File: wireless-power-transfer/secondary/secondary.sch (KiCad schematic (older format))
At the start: 9 parts, among them J1 Screw_Terminal_1x02, J2 Screw_Terminal_1x02, U1 LM7812CT

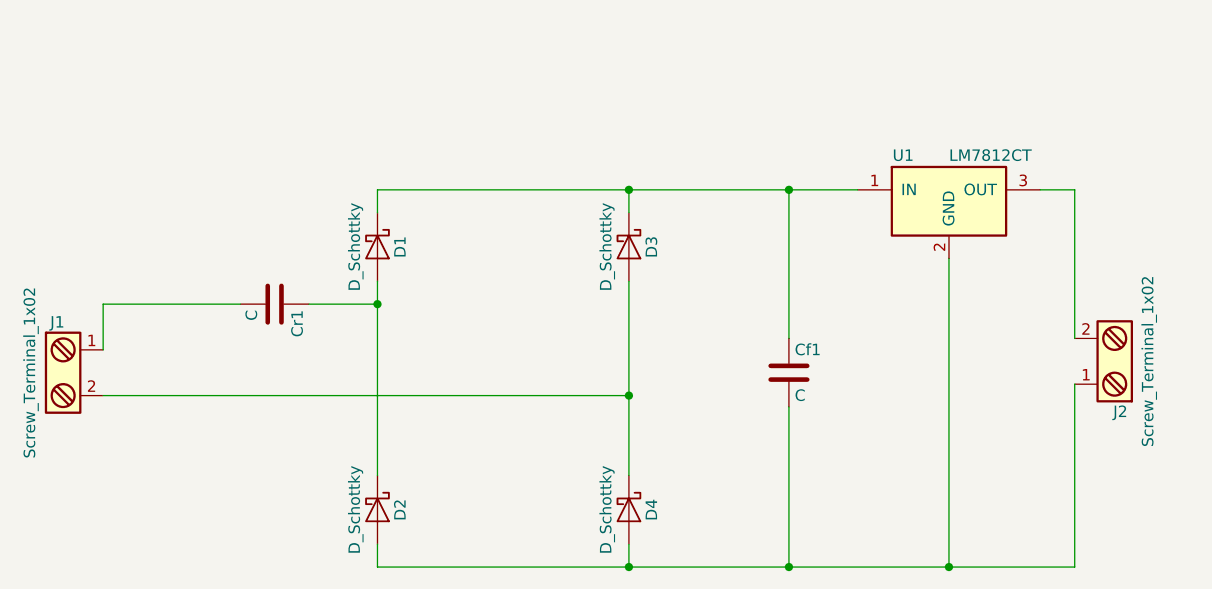
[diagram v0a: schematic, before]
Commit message: Added pdf sheets and modified layout according with the school standard for TFGs.
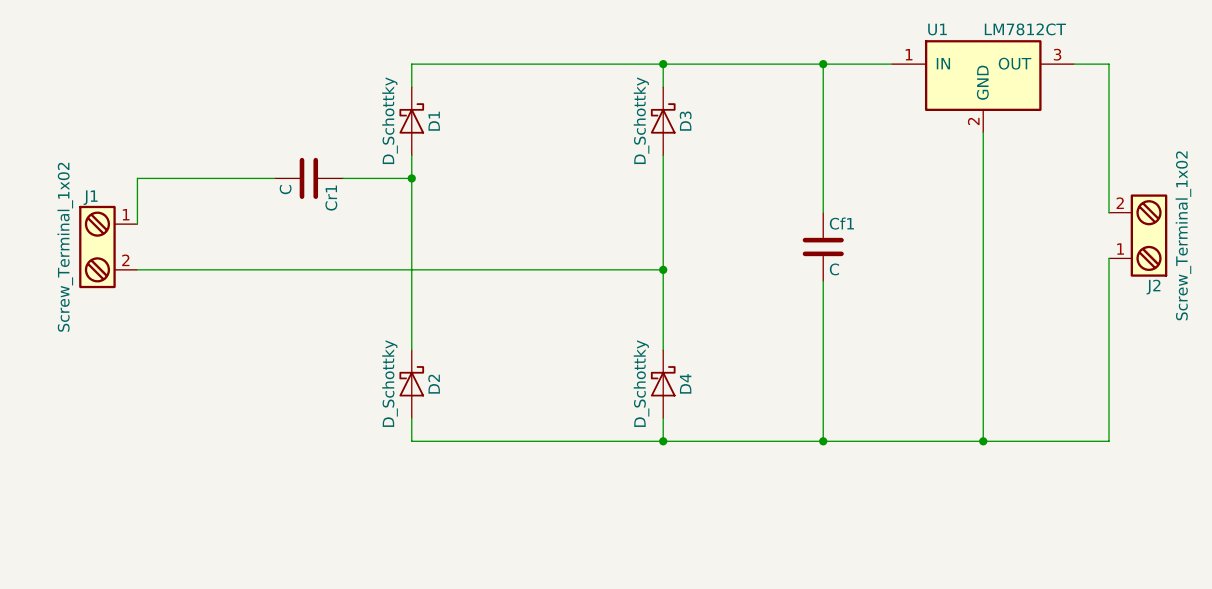
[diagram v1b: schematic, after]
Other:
- moved on the sheet: Cf1, Cr1, D1, D2, D3, D4, J1, J2, U1
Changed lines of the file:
@@
 L D_Schottky D1
 U 1 1 59E7A3A2
-P 4400 3100
-F 0 "D1" H 4400 3200 50  0000 C CNN
-F 1 "D_Schottky" H 4400 3000 50  0000 C CNN
-F 2 "Diodes_THT:D_DO-201AD_P12.70mm_Horizontal" H 4400 3100 50  0001 C CNN
-F 3 "" H 4400 3100 50  0001 C CNN
-	1    4400 3100
+P 4550 2550
+F 0 "D1" H 4550 2650 50  0000 C CNN
+F 1 "D_Schottky" H 4550 2450 50  0000 C CNN
+F 2 "Diodes_THT:D_DO-201AD_P12.70mm_Horizontal" H 4550 2550 50  0001 C CNN
+F 3 "" H 4550 2550 50  0001 C CNN
+	1    4550 2550
 	0    1    1    0
 $EndComp
@@
 L D_Schottky D2
 U 1 1 59E7A526
-P 4400 4250
-F 0 "D2" H 4400 4350 50  0000 C CNN
-F 1 "D_Schottky" H 4400 4150 50  0000 C CNN
-F 2 "Diodes_THT:D_DO-201AD_P12.70mm_Horizontal" H 4400 4250 50  0001 C CNN
-F 3 "" H 4400 4250 50  0001 C CNN
-	1    4400 4250
+P 4550 3700
+F 0 "D2" H 4550 3800 50  0000 C CNN
+F 1 "D_Schottky" H 4550 3600 50  0000 C CNN
+F 2 "Diodes_THT:D_DO-201AD_P12.70mm_Horizontal" H 4550 3700 50  0001 C CNN
+F 3 "" H 4550 3700 50  0001 C CNN
+	1    4550 3700
 	0    1    1    0
 $EndComp
@@
 L D_Schottky D3
 U 1 1 59E7A56E
-P 5500 3100
-F 0 "D3" H 5500 3200 50  0000 C CNN
-F 1 "D_Schottky" H 5500 3000 50  0000 C CNN
-F 2 "Diodes_THT:D_DO-201AD_P12.70mm_Horizontal" H 5500 3100 50  0001 C CNN
-F 3 "" H 5500 3100 50  0001 C CNN
-	1    5500 3100
+P 5650 2550
+F 0 "D3" H 5650 2650 50  0000 C CNN
+F 1 "D_Schottky" H 5650 2450 50  0000 C CNN
+F 2 "Diodes_THT:D_DO-201AD_P12.70mm_Horizontal" H 5650 2550 50  0001 C CNN
+F 3 "" H 5650 2550 50  0001 C CNN
+	1    5650 2550
 	0    1    1    0
 $EndComp
@@
 L D_Schottky D4
 U 1 1 59E7A5B1
-P 5500 4250
-F 0 "D4" H 5500 4350 50  0000 C CNN
-F 1 "D_Schottky" H 5500 4150 50  0000 C CNN
-F 2 "Diodes_THT:D_DO-201AD_P12.70mm_Horizontal" H 5500 4250 50  0001 C CNN
-F 3 "" H 5500 4250 50  0001 C CNN
-	1    5500 4250
+P 5650 3700
+F 0 "D4" H 5650 3800 50  0000 C CNN
+F 1 "D_Schottky" H 5650 3600 50  0000 C CNN
+F 2 "Diodes_THT:D_DO-201AD_P12.70mm_Horizontal" H 5650 3700 50  0001 C CNN
+F 3 "" H 5650 3700 50  0001 C CNN
+	1    5650 3700
 	0    1    1    0
 $EndComp
@@
 L C Cr1
 U 1 1 59E7A649
-P 3950 3350
-F 0 "Cr1" H 3975 3450 50  0000 L CNN
-F 1 "C" H 3975 3250 50  0000 L CNN
-F 2 "Capacitors_THT:C_Axial_L5.1mm_D3.1mm_P7.50mm_Horizontal" H 3988 3200 50  0001 C CNN
-F 3 "" H 3950 3350 50  0001 C CNN
-	1    3950 3350
+P 4100 2800
+F 0 "Cr1" H 4125 2900 50  0000 L CNN
+F 1 "C" H 4125 2700 50  0000 L CNN
+F 2 "Capacitors_THT:C_Axial_L5.1mm_D3.1mm_P7.50mm_Horizontal" H 4138 2650 50  0001 C CNN
+F 3 "" H 4100 2800 50  0001 C CNN
+	1    4100 2800
 	0    1    1    0
 $EndComp
@@
 L Screw_Terminal_1x02 J1
 U 1 1 59E7A6B3
-P 3000 3650
-F 0 "J1" H 3000 3900 50  0000 C TNN
-F 1 "Screw_Terminal_1x02" V 2850 3650 50  0000 C TNN
-F 2 "Connectors_Terminal_Blocks:TerminalBlock_Pheonix_MKDS1.5-2pol" H 3000 3425 50  0001 C CNN
-F 3 "" H 2975 3650 50  0001 C CNN
-	1    3000 3650
+P 3150 3100
+F 0 "J1" H 3150 3350 50  0000 C TNN
+F 1 "Screw_Terminal_1x02" V 3000 3100 50  0000 C TNN
+F 2 "Connectors_Terminal_Blocks:TerminalBlock_Pheonix_MKDS1.5-2pol" H 3150 2875 50  0001 C CNN
+F 3 "" H 3125 3100 50  0001 C CNN
+	1    3150 3100
 	1    0    0    -1
 $EndComp
@@
 L C Cf1
 U 1 1 59E7A7AC
-P 6200 3650
-F 0 "Cf1" H 6225 3750 50  0000 L CNN
-F 1 "C" H 6225 3550 50  0000 L CNN
-F 2 "Capacitors_THT:C_Rect_L13.0mm_W5.0mm_P10.00mm_FKS3_FKP3_MKS4" H 6238 3500 50  0001 C CNN
-F 3 "" H 6200 3650 50  0001 C CNN
-	1    6200 3650
+P 6350 3100
+F 0 "Cf1" H 6375 3200 50  0000 L CNN
+F 1 "C" H 6375 3000 50  0000 L CNN
+F 2 "Capacitors_THT:C_Rect_L13.0mm_W5.0mm_P10.00mm_FKS3_FKP3_MKS4" H 6388 2950 50  0001 C CNN
+F 3 "" H 6350 3100 50  0001 C CNN
+	1    6350 3100
 	1    0    0    -1
 $EndComp
@@
 L LM7812CT U1
 U 1 1 59E7A939
-P 6900 2900
-F 0 "U1" H 6700 3100 50  0000 C CNN
-F 1 "LM7812CT" H 6900 3100 50  0000 L CNN
-F 2 "TO_SOT_Packages_THT:TO-220-3_Vertical" H 6900 3000 50  0001 C CIN
-F 3 "" H 6900 2900 50  0001 C CNN
-	1    6900 2900
+P 7050 2350
+F 0 "U1" H 6850 2550 50  0000 C CNN
+F 1 "LM7812CT" H 7050 2550 50  0000 L CNN
+F 2 "TO_SOT_Packages_THT:TO-220-3_Vertical" H 7050 2450 50  0001 C CIN
+F 3 "" H 7050 2350 50  0001 C CNN
+	1    7050 2350
 	1    0    0    -1
 $EndComp
 Wire Wire Line
-	4400 4100 4400 3250
+	4550 3550 4550 2700
 Wire Wire Line
-	5500 3250 5500 4100
+	5650 2700 5650 3550
 Wire Wire Line
-	3200 3550 3200 3350
+	3350 3000 3350 2800
 Wire Wire Line
-	3200 3350 3800 3350
+	3350 2800 3950 2800
 Wire Wire Line
-	4400 2950 4400 2850
+	4550 2400 4550 2300
 Wire Wire Line
-	4400 2850 6500 2850
+	4550 2300 6650 2300
 Wire Wire Line
-	5500 2850 5500 2950
+	5650 2300 5650 2400
 Wire Wire Line
-	4400 4400 4400 4500
+	4550 3850 4550 3950
 Wire Wire Line
-	4400 4500 7450 4500
+	4550 3950 7600 3950
 Wire Wire Line
-	5500 4500 5500 4400
+	5650 3950 5650 3850
 Wire Wire Line
-	4100 3350 4400 3350
-Connection ~ 4400 3350
+	4250 2800 4550 2800
+Connection ~ 4550 2800
 Wire Wire Line
-	3200 3750 5500 3750
-Connection ~ 5500 3750
+	3350 3200 5650 3200
+Connection ~ 5650 3200
 Wire Wire Line
-	6200 2850 6200 3500
-Connection ~ 5500 2850
+	6350 2300 6350 2950
+Connection ~ 5650 2300
 Wire Wire Line
-	6200 4500 6200 3800
-Connection ~ 5500 4500
-Connection ~ 6200 2850
+	6350 3950 6350 3250
+Connection ~ 5650 3950
+Connection ~ 6350 2300
 Wire Wire Line
-	6900 4500 6900 3150
-Connection ~ 6200 4500
+	7050 3950 7050 2600
+Connection ~ 6350 3950
 $Comp
 L Screw_Terminal_1x02 J2
 U 1 1 59E7AA22
-P 7650 3600
-F 0 "J2" H 7650 3850 50  0000 C TNN
-F 1 "Screw_Terminal_1x02" V 7500 3600 50  0000 C TNN
-F 2 "Connectors_Terminal_Blocks:TerminalBlock_Pheonix_MKDS1.5-2pol" H 7650 3375 50  0001 C CNN
-F 3 "" H 7625 3600 50  0001 C CNN
-	1    7650 3600
+P 7800 3050
+F 0 "J2" H 7800 3300 50  0000 C TNN
+F 1 "Screw_Terminal_1x02" V 7650 3050 50  0000 C TNN
+F 2 "Connectors_Terminal_Blocks:TerminalBlock_Pheonix_MKDS1.5-2pol" H 7800 2825 50  0001 C CNN
+F 3 "" H 7775 3050 50  0001 C CNN
+	1    7800 3050
 	-1   0    0    1
 $EndComp
 Wire Wire Line
-	7300 2850 7450 2850
+	7450 2300 7600 2300
 Wire Wire Line
-	7450 2850 7450 3500
+	7600 2300 7600 2950
 Wire Wire Line
-	7450 4500 7450 3700
-Connection ~ 6900 4500
+	7600 3950 7600 3150
+Connection ~ 7050 3950
 $EndSCHEMATC

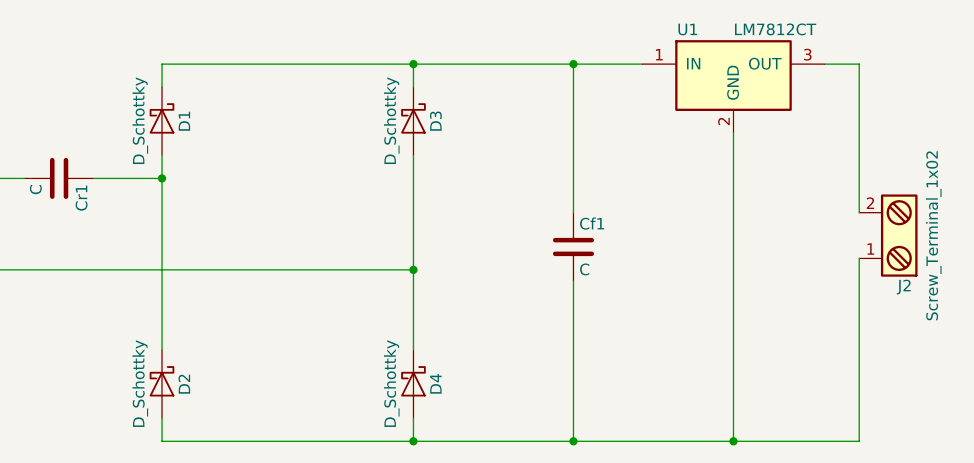
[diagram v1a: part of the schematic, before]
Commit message: Modified secondary PCB for better fitting in the car.
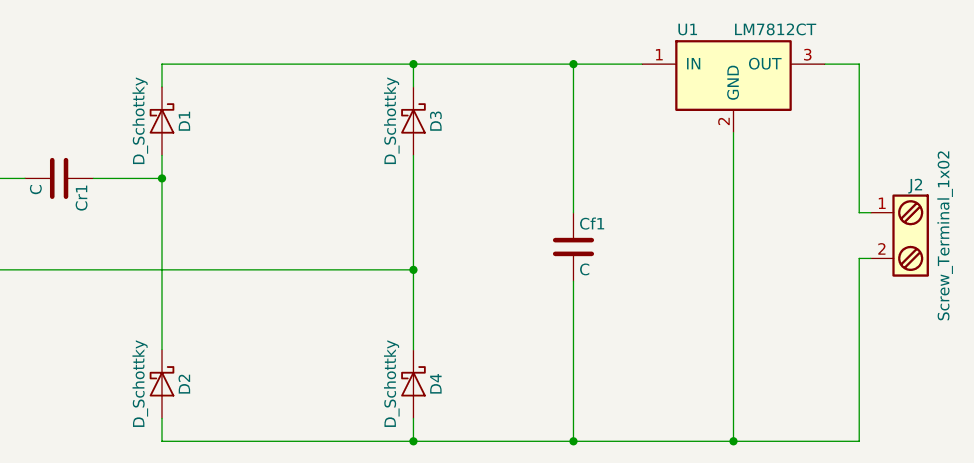
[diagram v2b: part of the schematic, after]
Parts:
- Cf1: footprint Capacitors_THT:C_Rect_L13.0mm_W5.0mm_P10.00mm_FKS3_FKP3_MKS4 -> Capacitors_THT:CP_Radial_D8.0mm_P3.50mm
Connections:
- net at Cf1.2, D2.2 (A), D4.2 (A)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: now also J2.2; no longer J2.1
- net at U1.3 (OUT): now also J2.1; no longer J2.2
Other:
- moved on the sheet: J2
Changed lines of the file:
@@
 F 0 "Cf1" H 6375 3200 50  0000 L CNN
 F 1 "C" H 6375 3000 50  0000 L CNN
-F 2 "Capacitors_THT:C_Rect_L13.0mm_W5.0mm_P10.00mm_FKS3_FKP3_MKS4" H 6388 2950 50  0001 C CNN
+F 2 "Capacitors_THT:CP_Radial_D8.0mm_P3.50mm" H 6388 2950 50  0001 C CNN
 F 3 "" H 6350 3100 50  0001 C CNN
 	1    6350 3100
@@
 $EndComp
 Wire Wire Line
-	4550 3550 4550 2700
+	4550 2700 4550 3550
 Wire Wire Line
 	5650 2700 5650 3550
@@
 L Screw_Terminal_1x02 J2
 U 1 1 59E7AA22
-P 7800 3050
-F 0 "J2" H 7800 3300 50  0000 C TNN
-F 1 "Screw_Terminal_1x02" V 7650 3050 50  0000 C TNN
-F 2 "Connectors_Terminal_Blocks:TerminalBlock_Pheonix_MKDS1.5-2pol" H 7800 2825 50  0001 C CNN
-F 3 "" H 7775 3050 50  0001 C CNN
-	1    7800 3050
-	-1   0    0    1
+P 7850 3050
+F 0 "J2" H 7850 3300 50  0000 C TNN
+F 1 "Screw_Terminal_1x02" V 7700 3050 50  0000 C TNN
+F 2 "Connectors_Terminal_Blocks:TerminalBlock_Pheonix_MKDS1.5-2pol" H 7850 2825 50  0001 C CNN
+F 3 "" H 7825 3050 50  0001 C CNN
+	1    7850 3050
+	-1   0    0    -1
 $EndComp
 Wire Wire Line
 	7450 2300 7600 2300
+Connection ~ 7050 3950
 Wire Wire Line
 	7600 2300 7600 2950
 Wire Wire Line
-	7600 3950 7600 3150
-Connection ~ 7050 3950
+	7600 2950 7650 2950
+Wire Wire Line
+	7650 3150 7600 3150
+Wire Wire Line
+	7600 3150 7600 3950
 $EndSCHEMATC

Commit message: PDFs created with schematics and PCB layers for front and back sides.
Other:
- note added: "5/7"
- moved on the sheet: Cf1, Cr1, D1, D2, D3, D4, J1, J2, U1
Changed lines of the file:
@@
 EELAYER 25 0
 EELAYER END
-$Descr A4 11693 8268
+$Descr A4 8268 11693 portrait
 encoding utf-8
 Sheet 1 1
@@
 L D_Schottky D1
 U 1 1 59E7A3A2
-P 4550 2550
-F 0 "D1" H 4550 2650 50  0000 C CNN
-F 1 "D_Schottky" H 4550 2450 50  0000 C CNN
-F 2 "Diodes_THT:D_DO-201AD_P12.70mm_Horizontal" H 4550 2550 50  0001 C CNN
-F 3 "" H 4550 2550 50  0001 C CNN
-	1    4550 2550
+P 3175 4275
+F 0 "D1" H 3175 4375 50  0000 C CNN
+F 1 "D_Schottky" H 3175 4175 50  0000 C CNN
+F 2 "Diodes_THT:D_DO-201AD_P12.70mm_Horizontal" H 3175 4275 50  0001 C CNN
+F 3 "" H 3175 4275 50  0001 C CNN
+	1    3175 4275
 	0    1    1    0
 $EndComp
@@
 L D_Schottky D2
 U 1 1 59E7A526
-P 4550 3700
-F 0 "D2" H 4550 3800 50  0000 C CNN
-F 1 "D_Schottky" H 4550 3600 50  0000 C CNN
-F 2 "Diodes_THT:D_DO-201AD_P12.70mm_Horizontal" H 4550 3700 50  0001 C CNN
-F 3 "" H 4550 3700 50  0001 C CNN
-	1    4550 3700
+P 3175 5425
+F 0 "D2" H 3175 5525 50  0000 C CNN
+F 1 "D_Schottky" H 3175 5325 50  0000 C CNN
+F 2 "Diodes_THT:D_DO-201AD_P12.70mm_Horizontal" H 3175 5425 50  0001 C CNN
+F 3 "" H 3175 5425 50  0001 C CNN
+	1    3175 5425
 	0    1    1    0
 $EndComp
@@
 L D_Schottky D3
 U 1 1 59E7A56E
-P 5650 2550
-F 0 "D3" H 5650 2650 50  0000 C CNN
-F 1 "D_Schottky" H 5650 2450 50  0000 C CNN
-F 2 "Diodes_THT:D_DO-201AD_P12.70mm_Horizontal" H 5650 2550 50  0001 C CNN
-F 3 "" H 5650 2550 50  0001 C CNN
-	1    5650 2550
+P 4275 4275
+F 0 "D3" H 4275 4375 50  0000 C CNN
+F 1 "D_Schottky" H 4275 4175 50  0000 C CNN
+F 2 "Diodes_THT:D_DO-201AD_P12.70mm_Horizontal" H 4275 4275 50  0001 C CNN
+F 3 "" H 4275 4275 50  0001 C CNN
+	1    4275 4275
 	0    1    1    0
 $EndComp
@@
 L D_Schottky D4
 U 1 1 59E7A5B1
-P 5650 3700
-F 0 "D4" H 5650 3800 50  0000 C CNN
-F 1 "D_Schottky" H 5650 3600 50  0000 C CNN
-F 2 "Diodes_THT:D_DO-201AD_P12.70mm_Horizontal" H 5650 3700 50  0001 C CNN
-F 3 "" H 5650 3700 50  0001 C CNN
-	1    5650 3700
+P 4275 5425
+F 0 "D4" H 4275 5525 50  0000 C CNN
+F 1 "D_Schottky" H 4275 5325 50  0000 C CNN
+F 2 "Diodes_THT:D_DO-201AD_P12.70mm_Horizontal" H 4275 5425 50  0001 C CNN
+F 3 "" H 4275 5425 50  0001 C CNN
+	1    4275 5425
 	0    1    1    0
 $EndComp
@@
 L C Cr1
 U 1 1 59E7A649
-P 4100 2800
-F 0 "Cr1" H 4125 2900 50  0000 L CNN
-F 1 "C" H 4125 2700 50  0000 L CNN
-F 2 "Capacitors_THT:C_Axial_L5.1mm_D3.1mm_P7.50mm_Horizontal" H 4138 2650 50  0001 C CNN
-F 3 "" H 4100 2800 50  0001 C CNN
-	1    4100 2800
+P 2725 4525
+F 0 "Cr1" H 2750 4625 50  0000 L CNN
+F 1 "C" H 2750 4425 50  0000 L CNN
+F 2 "Capacitors_THT:C_Axial_L5.1mm_D3.1mm_P7.50mm_Horizontal" H 2763 4375 50  0001 C CNN
+F 3 "" H 2725 4525 50  0001 C CNN
+	1    2725 4525
 	0    1    1    0
 $EndComp
@@
 L Screw_Terminal_1x02 J1
 U 1 1 59E7A6B3
-P 3150 3100
-F 0 "J1" H 3150 3350 50  0000 C TNN
-F 1 "Screw_Terminal_1x02" V 3000 3100 50  0000 C TNN
-F 2 "Connectors_Terminal_Blocks:TerminalBlock_Pheonix_MKDS1.5-2pol" H 3150 2875 50  0001 C CNN
-F 3 "" H 3125 3100 50  0001 C CNN
-	1    3150 3100
+P 1775 4825
+F 0 "J1" H 1775 5075 50  0000 C TNN
+F 1 "Screw_Terminal_1x02" V 1625 4825 50  0000 C TNN
+F 2 "Connectors_Terminal_Blocks:TerminalBlock_Pheonix_MKDS1.5-2pol" H 1775 4600 50  0001 C CNN
+F 3 "" H 1750 4825 50  0001 C CNN
+	1    1775 4825
 	1    0    0    -1
 $EndComp
@@
 L C Cf1
 U 1 1 59E7A7AC
-P 6350 3100
-F 0 "Cf1" H 6375 3200 50  0000 L CNN
-F 1 "C" H 6375 3000 50  0000 L CNN
-F 2 "Capacitors_THT:CP_Radial_D8.0mm_P3.50mm" H 6388 2950 50  0001 C CNN
-F 3 "" H 6350 3100 50  0001 C CNN
-	1    6350 3100
+P 4975 4825
+F 0 "Cf1" H 5000 4925 50  0000 L CNN
+F 1 "C" H 5000 4725 50  0000 L CNN
+F 2 "Capacitors_THT:CP_Radial_D8.0mm_P3.50mm" H 5013 4675 50  0001 C CNN
+F 3 "" H 4975 4825 50  0001 C CNN
+	1    4975 4825
 	1    0    0    -1
 $EndComp
@@
 L LM7812CT U1
 U 1 1 59E7A939
-P 7050 2350
-F 0 "U1" H 6850 2550 50  0000 C CNN
-F 1 "LM7812CT" H 7050 2550 50  0000 L CNN
-F 2 "TO_SOT_Packages_THT:TO-220-3_Vertical" H 7050 2450 50  0001 C CIN
-F 3 "" H 7050 2350 50  0001 C CNN
-	1    7050 2350
+P 5675 4075
+F 0 "U1" H 5475 4275 50  0000 C CNN
+F 1 "LM7812CT" H 5675 4275 50  0000 L CNN
+F 2 "TO_SOT_Packages_THT:TO-220-3_Vertical" H 5675 4175 50  0001 C CIN
+F 3 "" H 5675 4075 50  0001 C CNN
+	1    5675 4075
 	1    0    0    -1
 $EndComp
 Wire Wire Line
-	4550 2700 4550 3550
+	3175 4425 3175 5275
 Wire Wire Line
-	5650 2700 5650 3550
+	4275 4425 4275 5275
 Wire Wire Line
-	3350 3000 3350 2800
+	1975 4725 1975 4525
 Wire Wire Line
-	3350 2800 3950 2800
+	1975 4525 2575 4525
 Wire Wire Line
-	4550 2400 4550 2300
+	3175 4125 3175 4025
 Wire Wire Line
-	4550 2300 6650 2300
+	3175 4025 5275 4025
 Wire Wire Line
-	5650 2300 5650 2400
+	4275 4025 4275 4125
 Wire Wire Line
-	4550 3850 4550 3950
+	3175 5575 3175 5675
 Wire Wire Line
-	4550 3950 7600 3950
+	3175 5675 6225 5675
 Wire Wire Line
-	5650 3950 5650 3850
+	4275 5675 4275 5575
 Wire Wire Line
-	4250 2800 4550 2800
-Connection ~ 4550 2800
+	2875 4525 3175 4525
+Connection ~ 3175 4525
 Wire Wire Line
-	3350 3200 5650 3200
-Connection ~ 5650 3200
+	1975 4925 4275 4925
+Connection ~ 4275 4925
 Wire Wire Line
-	6350 2300 6350 2950
-Connection ~ 5650 2300
+	4975 4025 4975 4675
+Connection ~ 4275 4025
 Wire Wire Line
-	6350 3950 6350 3250
-Connection ~ 5650 3950
-Connection ~ 6350 2300
+	4975 5675 4975 4975
+Connection ~ 4275 5675
+Connection ~ 4975 4025
 Wire Wire Line
-	7050 3950 7050 2600
-Connection ~ 6350 3950
+	5675 5675 5675 4325
+Connection ~ 4975 5675
 $Comp
 L Screw_Terminal_1x02 J2
 U 1 1 59E7AA22
-P 7850 3050
-F 0 "J2" H 7850 3300 50  0000 C TNN
-F 1 "Screw_Terminal_1x02" V 7700 3050 50  0000 C TNN
-F 2 "Connectors_Terminal_Blocks:TerminalBlock_Pheonix_MKDS1.5-2pol" H 7850 2825 50  0001 C CNN
-F 3 "" H 7825 3050 50  0001 C CNN
-	1    7850 3050
+P 6475 4775
+F 0 "J2" H 6475 5025 50  0000 C TNN
+F 1 "Screw_Terminal_1x02" V 6325 4775 50  0000 C TNN
+F 2 "Connectors_Terminal_Blocks:TerminalBlock_Pheonix_MKDS1.5-2pol" H 6475 4550 50  0001 C CNN
+F 3 "" H 6450 4775 50  0001 C CNN
+	1    6475 4775
 	-1   0    0    -1
 $EndComp
 Wire Wire Line
-	7450 2300 7600 2300
-Connection ~ 7050 3950
+	6075 4025 6225 4025
+Connection ~ 5675 5675
 Wire Wire Line
-	7600 2300 7600 2950
+	6225 4025 6225 4675
 Wire Wire Line
-	7600 2950 7650 2950
+	6225 4675 6275 4675
 Wire Wire Line
-	7650 3150 7600 3150
+	6275 4875 6225 4875
 Wire Wire Line
-	7600 3150 7600 3950
+	6225 4875 6225 5675
+Text Notes 6850 11000 0    118  ~ 0
+5/7
 $EndSCHEMATC
